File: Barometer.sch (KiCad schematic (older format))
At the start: 5 parts, among them U9 BMP388

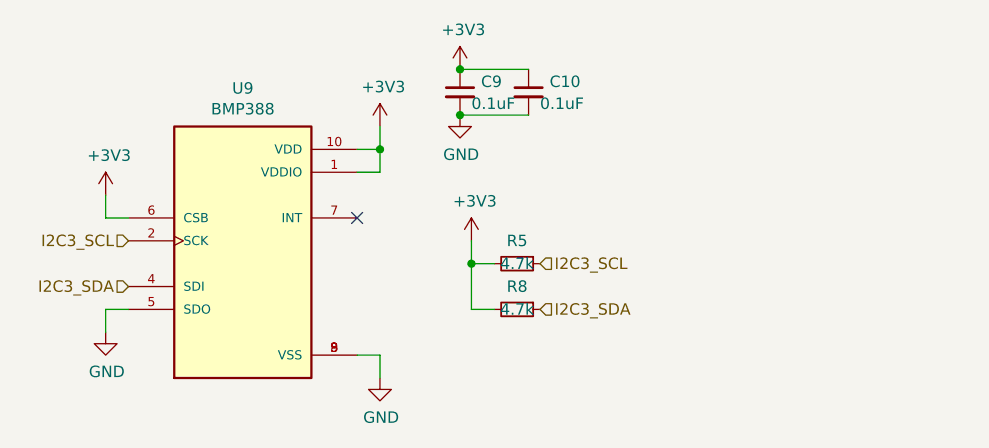
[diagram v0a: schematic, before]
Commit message: Updated the schematics to include pictures
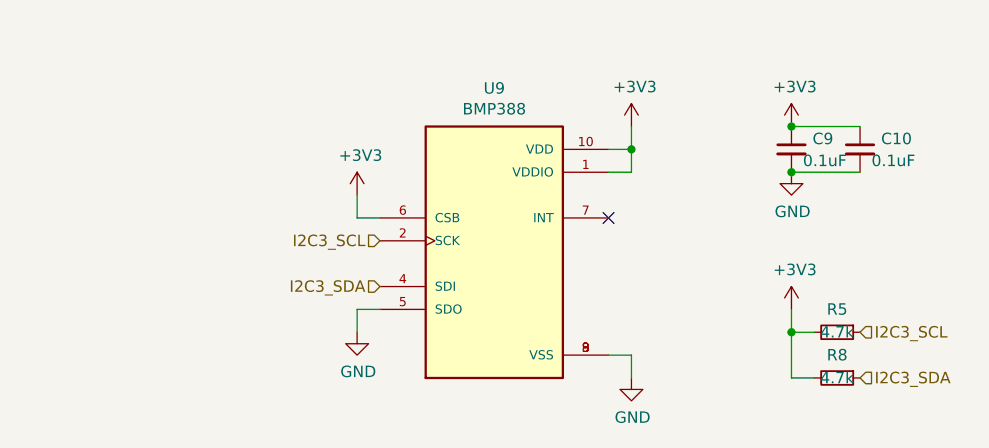
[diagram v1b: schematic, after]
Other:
- moved on the sheet: C10, C9, R5, R8, U9

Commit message: Rerouted a bit
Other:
- note added: "Barometer"
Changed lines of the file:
@@
 EndData
 $EndBitmap
+Text Notes 3950 1750 0    591  ~ 118
+Barometer
 $EndSCHEMATC
